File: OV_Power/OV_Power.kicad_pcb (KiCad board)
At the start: 4 copper layers, 90 x 60 mm, 78 parts, among them CN1 CONN_HEADER_R_A_2POS_2.5MM, J1 Kycon_kpjx-4s, J2 Conn_HDR_2x10_latching, J3 532530670, J4 SpadeLug, J5 SpadeLug, J6 CONN_HEADER_2.54X2_MOLEX_KK_S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, J7 CONN_HEADER_2.54X2_MOLEX_KK_S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, Q1 SSM3K341R, Q2 2N7002BK, Q3 SZNUD3124LT1G, Q4 SZNUD3124LT1G, U1 LT3796, U2 LT1936, U3 LT6106, U4 VNH5019ATR-E, U7 LTC4416, U8 AOSD21307, U9 AOSD21307

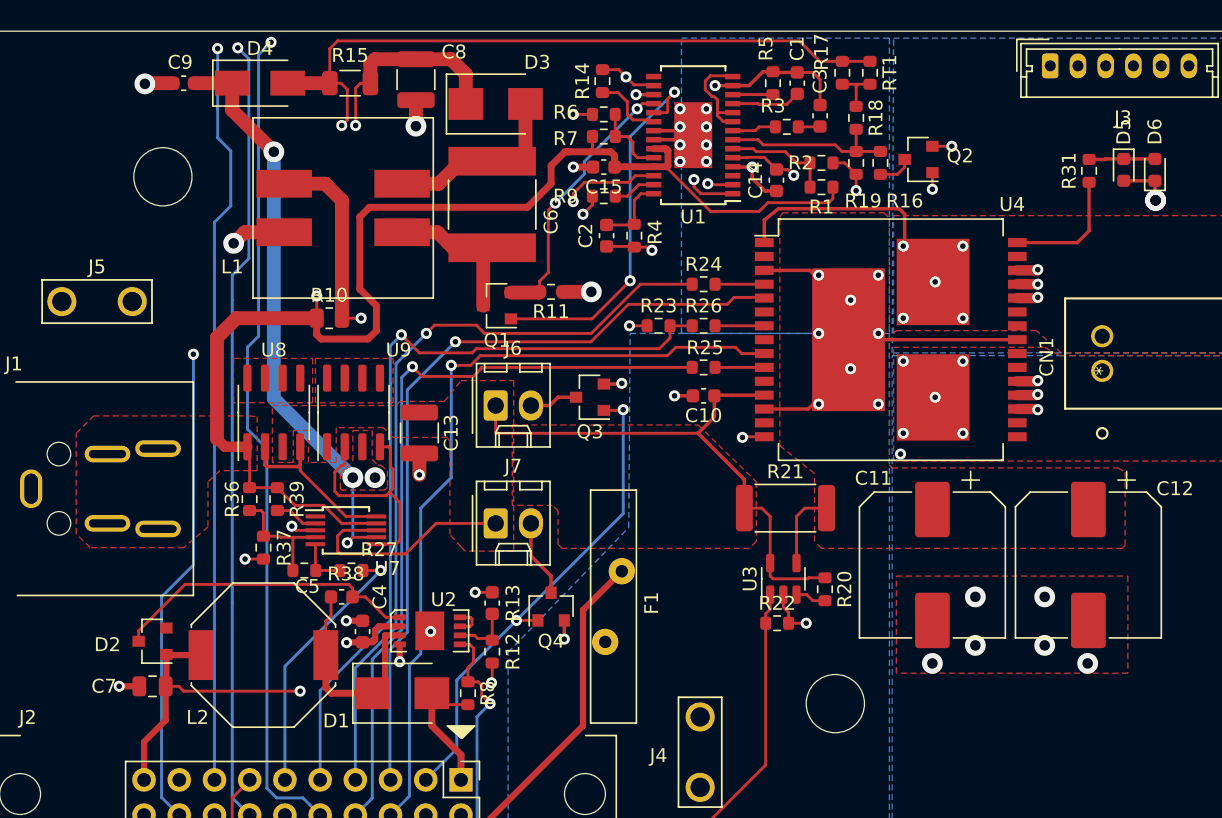
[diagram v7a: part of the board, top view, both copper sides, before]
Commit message: Some cleanups of the silkscreen on the power board...
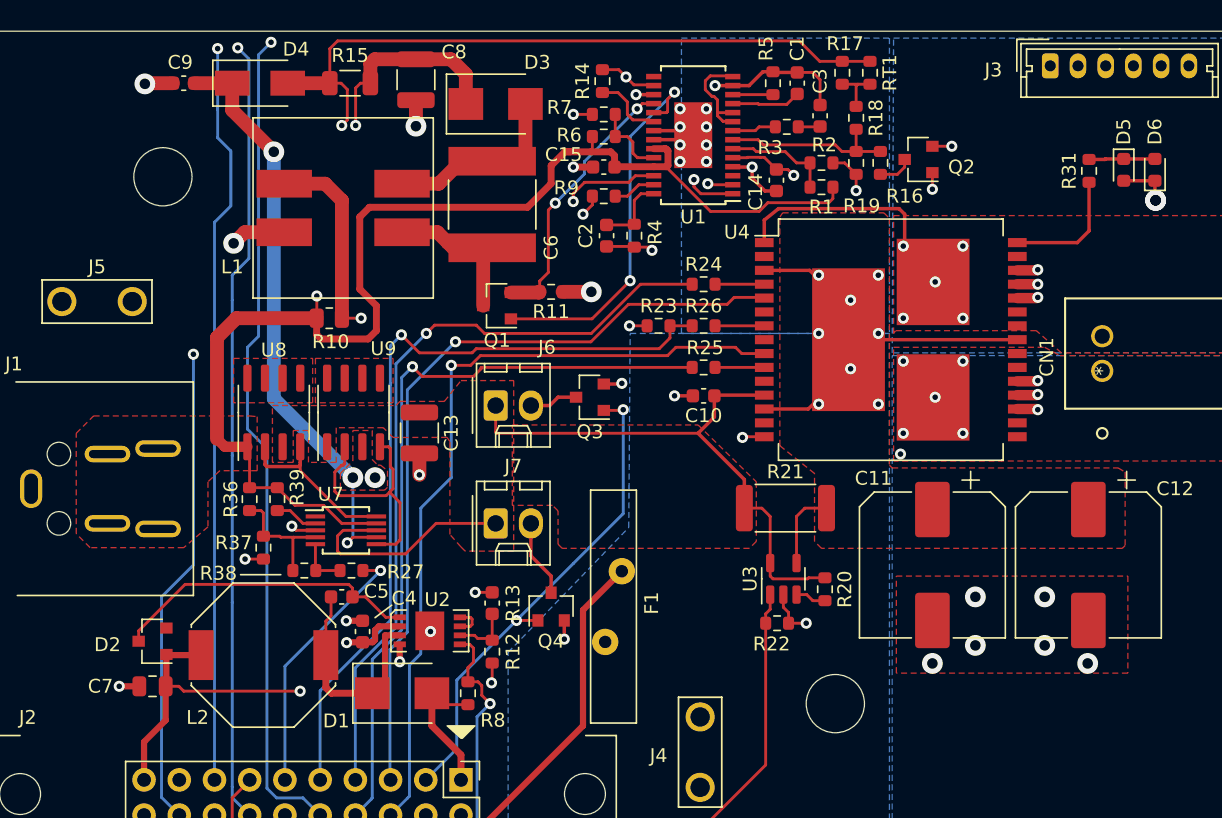
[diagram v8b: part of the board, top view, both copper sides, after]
